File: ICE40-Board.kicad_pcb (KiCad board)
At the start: 4 copper layers, 134.4 x 58 mm, 83 parts, among them SW1 SW_Push, SW2 SW_Push, U1 ADP122AUJZ-3.3-R7, U10 FT4222HQ, U11 74LS125, U12 74LS126, U2 ADP1712AUJZ-2.5, U3 ADP1712AUJZ-1.2, U4 Barrel_Jack, U5 W25X20CLSNIG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

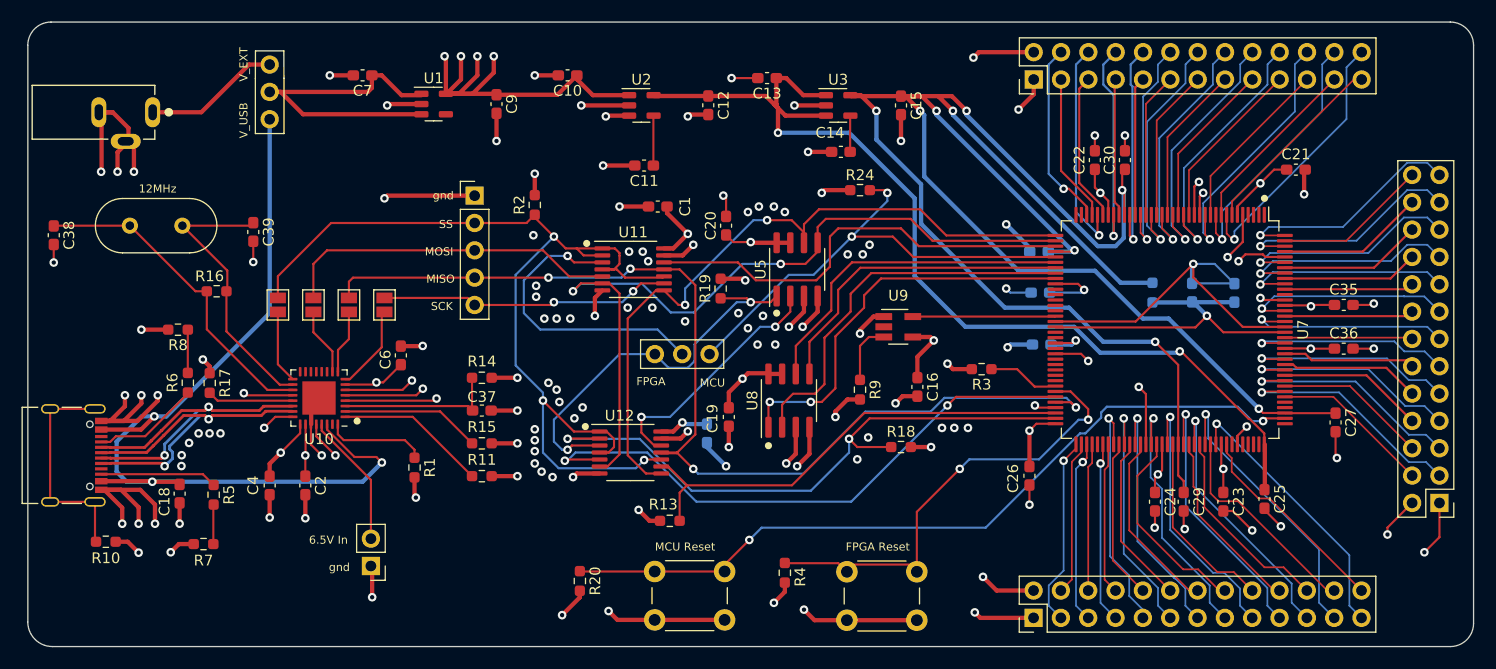
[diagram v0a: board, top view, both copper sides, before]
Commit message: Placed vias around SPI lines, placed main oscillator closer to FPGA
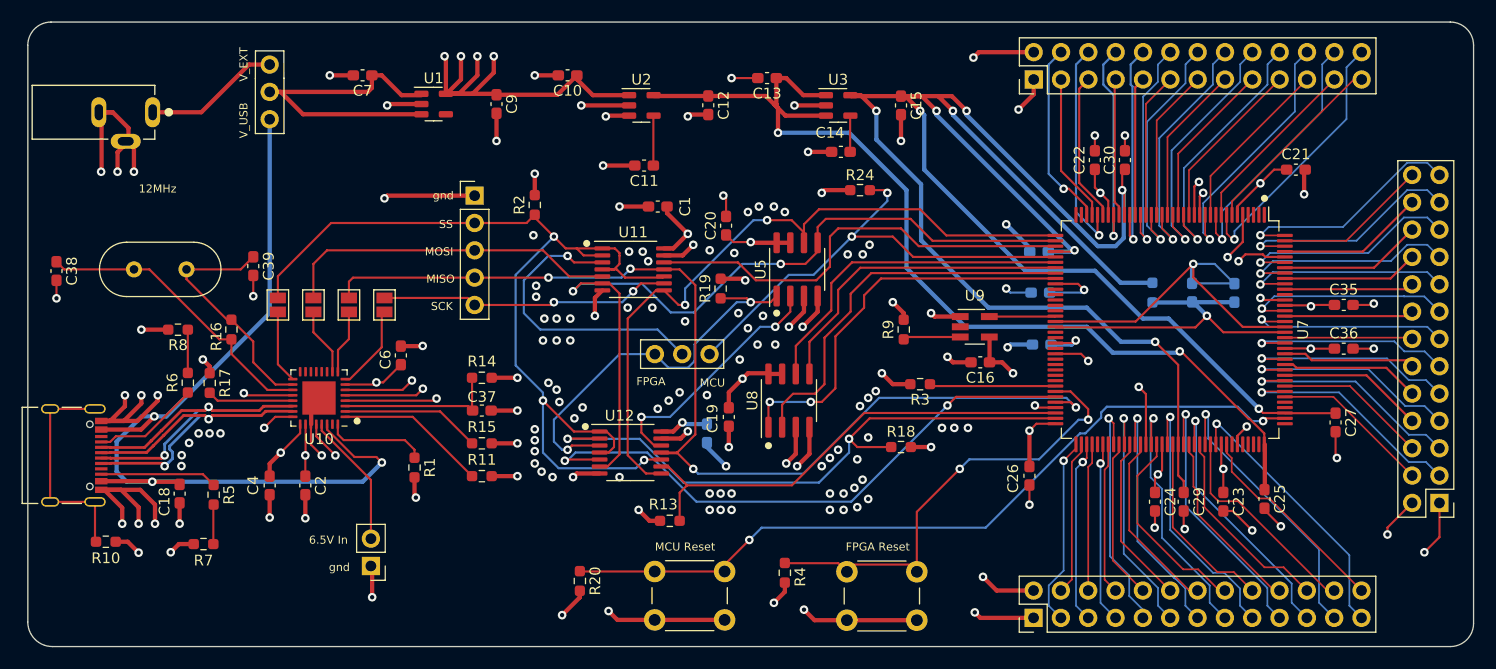
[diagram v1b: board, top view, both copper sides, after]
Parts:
- moved U9 7.11 mm to (108.7, 45.0)
- moved R9 6.91 mm to (102.1, 45.2), turned to 90 degrees
- moved C16 6.27 mm to (109.2, 48.3), turned to 180 degrees
- moved R3 5.88 mm to (103.6, 50.3)
- moved FT_Crystal1 4.08 mm to (30.6, 39.6)
- moved R16 3.81 mm to (39.6, 45.2), turned to 90 degrees
- moved C38 3.34 mm to (23.4, 39.8)
- moved C39 3.18 mm to (41.7, 39.3)
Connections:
- net /MCU_RESET renamed Net-(R20-Pad1)
- net Net-(U7-Pad52) renamed /FPGA_CLK
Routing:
- net /FPGA_CLK: track 13.3 -> 6.16 mm
- net Net-(R3-Pad1): track 5.86 -> 11.7 mm
- net Net-(C39-Pad1): track 26.5 -> 22.7 mm
- net Net-(C38-Pad1): track 30.6 -> 27.7 mm
- net +3V3: track 207.2 -> 205.4 mm
- net /SS_FPGA: track 58.1 -> 57.5 mm
- net +1V2: track 207.2 -> 207.7 mm
- net GND: track 265.9 -> 265.8 mm, vias 123 -> 154

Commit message: Version 1.0 completed
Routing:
- net +1V2: track 207.7 -> 71.3 mm, vias 9 -> 8
- net +3V3: track 205.4 -> 205.9 mm
- added copper zone on B.Cu, net +1V2
